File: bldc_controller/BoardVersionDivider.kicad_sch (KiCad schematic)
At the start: 2 parts

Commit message: might have fixed net issue, added dxf and svgs
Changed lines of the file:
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@@
     (stroke (width 0) (type default))
   )
-  (polyline (pts (xy 183.515 132.08) (xy 119.38 132.08))
-    (stroke (width 0) (type default))
-  )
-  (polyline (pts (xy 152.4 113.03) (xy 152.4 120.65))
+  (polyline (pts (xy 149.86 111.76) (xy 149.86 119.38))
     (stroke (width 0) (type default))
   )
@@
     (stroke (width 0) (type default))
   )
-  (polyline (pts (xy 187.325 59.69) (xy 187.325 128.27))
-    (stroke (width 0) (type default))
-  )
   (wire (pts (xy 162.56 83.82) (xy 149.86 83.82))
-    (stroke (width 0) (type default))
-  )
-  (polyline (pts (xy 119.38 55.88) (xy 183.515 55.88))
     (stroke (width 0) (type default))
   )
@@
     (stroke (width 0) (type default))
   )
-  (polyline (pts (xy 142.24 116.84) (xy 162.56 116.84))
+  (polyline (pts (xy 139.7 115.57) (xy 160.02 115.57))
     (stroke (width 0) (type default))
   )
@@
     (stroke (width 0) (type default))
   )
-  (polyline (pts (xy 115.57 59.69) (xy 115.57 128.27))
-    (stroke (width 0) (type default))
+  (rectangle (start 104.14 49.53) (end 198.12 133.35)
+    (stroke (width 1) (type default) (color 200 200 200 1))
+    (fill (type none))
   )
-  (arc (start 187.325 128.27) (mid 186.2108 130.9673) (end 183.515 132.08)
+  (rectangle (start 139.7 111.76) (end 160.02 119.38)
     (stroke (width 0) (type default))
     (fill (type none))
   )
-  (arc (start 183.515 55.88) (mid 186.2073 56.9962) (end 187.325 59.69)
-    (stroke (width 0) (type default))
-    (fill (type none))
-  )
-  (rectangle (start 142.24 113.03) (end 162.56 120.65)
-    (stroke (width 0) (type default))
-    (fill (type none))
-  )
-  (arc (start 115.57 59.69) (mid 116.6859 56.9959) (end 119.38 55.88)
-    (stroke (width 0) (type default))
-    (fill (type none))
-  )
-  (arc (start 119.38 132.08) (mid 116.6845 130.9655) (end 115.57 128.27)
-    (stroke (width 0) (type default))
-    (fill (type none))
-  )
-  (text_box "Necessary to be compatible with moteus FW."
-    (at 115.57 133.35 0) (size 71.12 11.43)
+  (text_box "100k"
+    (at 149.86 111.76 0) (size 10.16 3.81)
     (stroke (width -0.0001) (type default))
     (fill (type none))
-    (effects (font (size 2.54 2.54) (color 0 0 0 1)) (justify bottom))
+    (effects (font (face "Arial") (size 1.27 1.27) (color 0 0 0 1)))
   )
-  (text_box "			TOP		BOT\n\nr1.1 r1.2	  x		100k\n\n     r1.3	100k	  x"
-    (at 128.905 109.22 0) (size 33.02 8.89)
+  (text_box "DESIGN NOTE:\nNecessary to be compatible with moteus FW."
+    (at 119.38 71.12 0) (size 26.67 8.89)
+    (stroke (width 0.8) (type solid) (color 255 165 0 1))
+    (fill (type none))
+    (effects (font (face "Arial") (size 1.27 1.27) (color 0 0 0 1)) (justify left top))
+  )
+  (text_box "BOTTOM"
+    (at 149.86 107.95 0) (size 10.16 3.81)
     (stroke (width -0.0001) (type default))
     (fill (type none))
-    (effects (font (size 1.27 1.27)) (justify left top))
+    (effects (font (face "Arial") (size 1.27 1.27) (color 0 0 0 1)))
   )
-  (text_box "Back to Top Level"
-    (at 265.43 166.37 0) (size 19.05 14.605)
-    (stroke (width 0) (type default) (color 0 0 0 1))
-    (fill (type color) (color 0 0 0 0.1))
-    (effects (font (size 2.54 2.54) (thickness 0.508) bold (color 0 0 0 1)) (href "#1"))
+  (text_box "x"
+    (at 139.7 111.76 0) (size 10.16 3.81)
+    (stroke (width -0.0001) (type default))
+    (fill (type none))
+    (effects (font (face "Arial") (size 1.27 1.27) (color 0 0 0 1)))
+  )
+  (text_box "[10] Misc - Board Version Divider"
+    (at 78.74 16.51 0) (size 137.16 12.7)
+    (stroke (width -0.0001) (type default))
+    (fill (type none))
+    (effects (font (face "Times New Roman") (size 6 6) (thickness 1.2) bold (color 162 22 34 1)))
+  )
+  (text_box "r1.3"
+    (at 129.54 115.57 0) (size 10.16 3.81)
+    (stroke (width -0.0001) (type default))
+    (fill (type none))
+    (effects (font (face "Arial") (size 1.27 1.27) (color 0 0 0 1)) (justify right))
+  )
+  (text_box "100k"
+    (at 139.7 115.57 0) (size 10.16 3.81)
+    (stroke (width -0.0001) (type default))
+    (fill (type none))
+    (effects (font (face "Arial") (size 1.27 1.27) (color 0 0 0 1)))
+  )
+  (text_box "TOP"
+    (at 139.7 107.95 0) (size 10.16 3.81)
+    (stroke (width -0.0001) (type default))
+    (fill (type none))
+    (effects (font (face "Arial") (size 1.27 1.27) (color 0 0 0 1)))
+  )
+  (text_box "x"
+    (at 149.86 115.57 0) (size 10.16 3.81)
+    (stroke (width -0.0001) (type default))
+    (fill (type none))
+    (effects (font (face "Arial") (size 1.27 1.27) (color 0 0 0 1)))
   )
   (text_box "Board Version Resistor Divider"
-    (at 118.11 120.65 0) (size 66.675 9.525)
+    (at 105.41 121.92 0) (size 91.44 9.525)
     (stroke (width -0.0001) (type default))
     (fill (type none))
-    (effects (font (size 2.54 2.54) (thickness 0.508) bold (color 0 0 0 1)) (justify bottom))
+    (effects (font (face "Times New Roman") (size 2.54 2.54) (thickness 0.508) bold (color 162 22 34 1)) (justify bottom))
+  )
+  (text_box "r1.1, r1.2"
+    (at 129.54 111.76 0) (size 10.16 3.81)
+    (stroke (width -0.0001) (type default))
+    (fill (type none))
+    (effects (font (face "Arial") (size 1.27 1.27) (color 0 0 0 1)) (justify right))
   )
   (hierarchical_label "BOARD_VERSION" (shape output) (at 162.56 83.82 0) (fields_autoplaced)
@@
     (instances
       (project "bldc_controller"
-        (path "/0650c7a8-acba-429c-9f8e-eec0baf0bc1c/6ac64cfc-cd02-4504-88c7-a17dadca0833"
+        (path "/0650c7a8-acba-429c-9f8e-eec0baf0bc1c/fede4c36-00cc-4d3d-b71c-5243ba232202/07dcaf51-abc9-470d-8bd8-30b1c54b6fbd"
           (reference "R44") (unit 1)
         )
@@
   (symbol (lib_id "power:+3V3") (at 149.86 64.77 0) (unit 1)
     (in_bom yes) (on_board yes) (dnp no) (fields_autoplaced)
-    (property "Reference" "#PWR070" (at 149.86 68.58 0)
+    (property "Reference" "#PWR059" (at 149.86 68.58 0)
       (effects (font (size 1.27 1.27)) hide)
     )
@@
     (instances
       (project "bldc_controller"
-        (path "/0650c7a8-acba-429c-9f8e-eec0baf0bc1c/6ac64cfc-cd02-4504-88c7-a17dadca0833"
-          (reference "#PWR070") (unit 1)
+        (path "/0650c7a8-acba-429c-9f8e-eec0baf0bc1c/fede4c36-00cc-4d3d-b71c-5243ba232202/07dcaf51-abc9-470d-8bd8-30b1c54b6fbd"
+          (reference "#PWR059") (unit 1)
         )
       )
@@
   (symbol (lib_id "power:GND") (at 149.86 100.33 0) (unit 1)
     (in_bom yes) (on_board yes) (dnp no) (fields_autoplaced)
-    (property "Reference" "#PWR071" (at 149.86 106.68 0)
+    (property "Reference" "#PWR060" (at 149.86 106.68 0)
       (effects (font (size 1.27 1.27)) hide)
     )
@@
     (instances
       (project "bldc_controller"
-        (path "/0650c7a8-acba-429c-9f8e-eec0baf0bc1c/6ac64cfc-cd02-4504-88c7-a17dadca0833"
-          (reference "#PWR071") (unit 1)
+        (path "/0650c7a8-acba-429c-9f8e-eec0baf0bc1c/fede4c36-00cc-4d3d-b71c-5243ba232202/07dcaf51-abc9-470d-8bd8-30b1c54b6fbd"
+          (reference "#PWR060") (unit 1)
         )
       )
@@
     (instances
       (project "bldc_controller"
-        (path "/0650c7a8-acba-429c-9f8e-eec0baf0bc1c/6ac64cfc-cd02-4504-88c7-a17dadca0833"
+        (path "/0650c7a8-acba-429c-9f8e-eec0baf0bc1c/fede4c36-00cc-4d3d-b71c-5243ba232202/07dcaf51-abc9-470d-8bd8-30b1c54b6fbd"
           (reference "R43") (unit 1)
         )

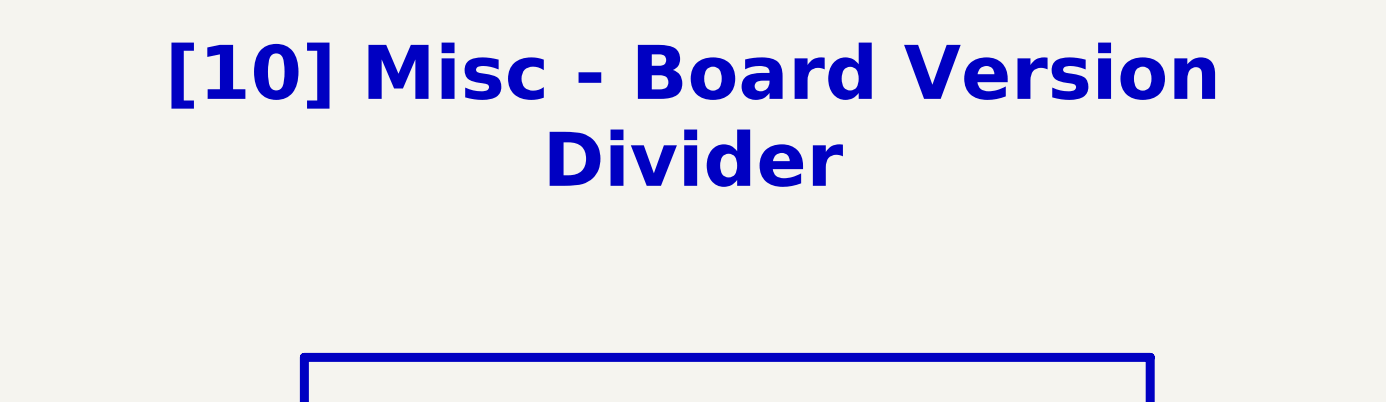
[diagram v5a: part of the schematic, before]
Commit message: Replaced 3v3 buck with WSON package alternative. Will back-annotate components
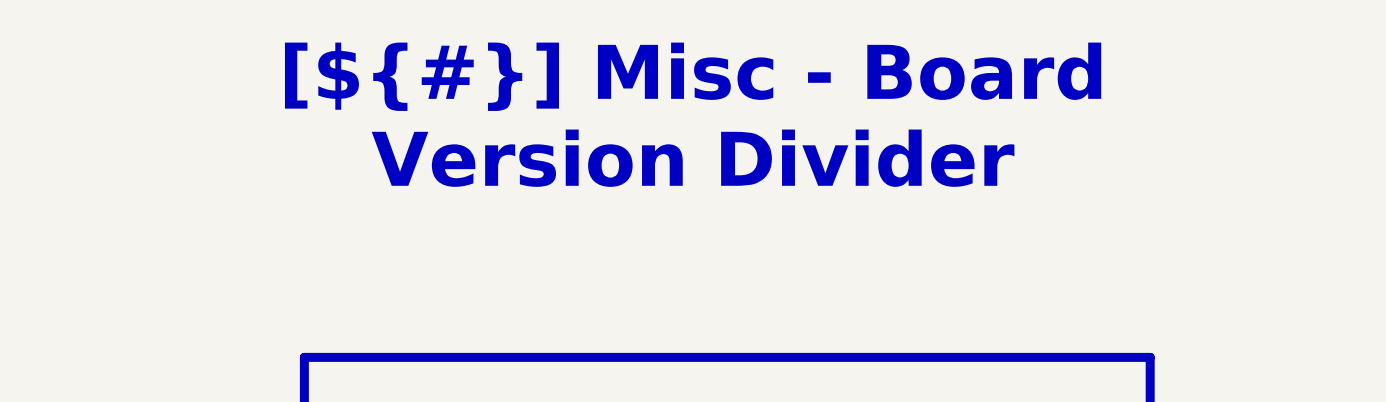
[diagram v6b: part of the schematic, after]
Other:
- company: EPFL Xplore -> ${COMPANY}
- title: Board Version Resistor Divider -> Misc - Board Version Divider
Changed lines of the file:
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@@
   (paper "A4")
   (title_block
-    (title "Board Version Resistor Divider")
+    (title "Misc - Board Version Divider")
     (date "2023-10-14")
-    (rev "1.0")
-    (company "EPFL Xplore")
-    (comment 3 "Author: Vincent Nguyen")
+    (rev "${REVISION}")
+    (company "${COMPANY}")
+    (comment 3 "Author: ${AUTHOR}")
   )
   (junction (at 149.86 83.82) (diameter 0) (color 0 0 0 0)
@@
   )
   (wire (pts (xy 149.86 100.33) (xy 149.86 96.52))
-    (stroke (width 0.381) (type default) (color 0 0 0 1))
+    (stroke (width 0) (type default))
   )
   (rectangle (start 104.14 49.53) (end 198.12 133.35)
@@
     (effects (font (face "Arial") (size 1.27 1.27) (color 0 0 0 1)))
   )
-  (text_box "[10] Misc - Board Version Divider"
+  (text_box "[${#}] ${TITLE}"
     (at 78.74 16.51 0) (size 137.16 12.7)
     (stroke (width -0.0001) (type default))

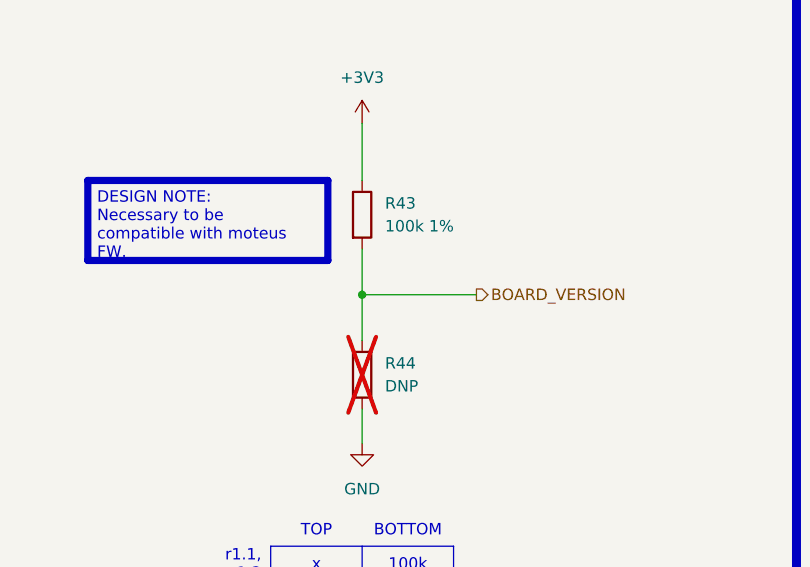
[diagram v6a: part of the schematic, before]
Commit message: routed all signals. TODO: redo all power polygons and ensure good return paths/reference. Added 3d models
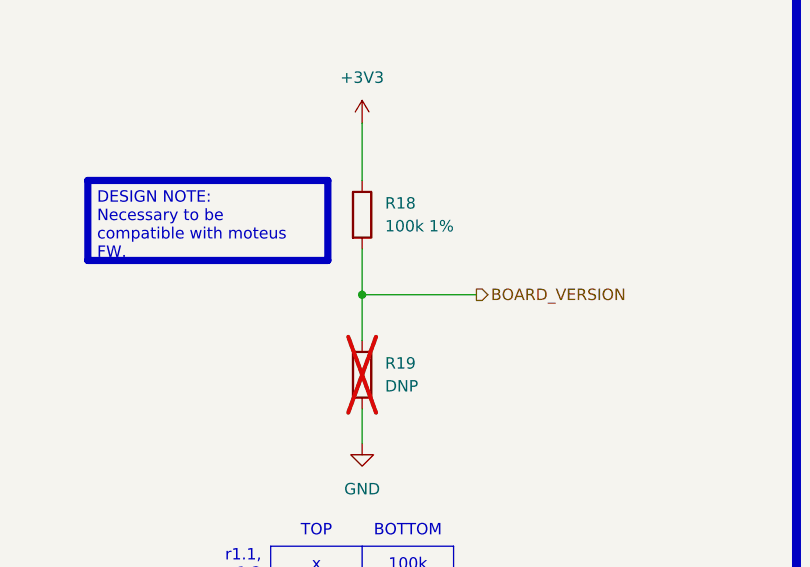
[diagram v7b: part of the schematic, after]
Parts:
- renumbered R43 to R18, R44 to R19
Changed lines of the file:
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@@
   (symbol (lib_id "Device:R") (at 149.86 92.71 0) (unit 1)
     (in_bom no) (on_board yes) (dnp yes) (fields_autoplaced)
-    (property "Reference" "R44" (at 152.4 91.44 0)
+    (property "Reference" "R19" (at 152.4 91.44 0)
       (effects (font (size 1.27 1.27)) (justify left))
     )
@@
       (project "bldc_controller"
         (path "/0650c7a8-acba-429c-9f8e-eec0baf0bc1c/fede4c36-00cc-4d3d-b71c-5243ba232202/07dcaf51-abc9-470d-8bd8-30b1c54b6fbd"
-          (reference "R44") (unit 1)
+          (reference "R19") (unit 1)
         )
       )
@@
   (symbol (lib_id "power:+3V3") (at 149.86 64.77 0) (unit 1)
     (in_bom yes) (on_board yes) (dnp no) (fields_autoplaced)
-    (property "Reference" "#PWR059" (at 149.86 68.58 0)
+    (property "Reference" "#PWR037" (at 149.86 68.58 0)
       (effects (font (size 1.27 1.27)) hide)
     )
@@
       (project "bldc_controller"
         (path "/0650c7a8-acba-429c-9f8e-eec0baf0bc1c/fede4c36-00cc-4d3d-b71c-5243ba232202/07dcaf51-abc9-470d-8bd8-30b1c54b6fbd"
-          (reference "#PWR059") (unit 1)
+          (reference "#PWR037") (unit 1)
         )
       )
@@
   (symbol (lib_id "power:GND") (at 149.86 100.33 0) (unit 1)
     (in_bom yes) (on_board yes) (dnp no) (fields_autoplaced)
-    (property "Reference" "#PWR060" (at 149.86 106.68 0)
+    (property "Reference" "#PWR038" (at 149.86 106.68 0)
       (effects (font (size 1.27 1.27)) hide)
     )
@@
       (project "bldc_controller"
         (path "/0650c7a8-acba-429c-9f8e-eec0baf0bc1c/fede4c36-00cc-4d3d-b71c-5243ba232202/07dcaf51-abc9-470d-8bd8-30b1c54b6fbd"
-          (reference "#PWR060") (unit 1)
+          (reference "#PWR038") (unit 1)
         )
       )
@@
   (symbol (lib_id "Device:R") (at 149.86 74.93 0) (unit 1)
     (in_bom yes) (on_board yes) (dnp no) (fields_autoplaced)
-    (property "Reference" "R43" (at 152.4 73.66 0)
+    (property "Reference" "R18" (at 152.4 73.66 0)
       (effects (font (size 1.27 1.27)) (justify left))
     )
@@
       (project "bldc_controller"
         (path "/0650c7a8-acba-429c-9f8e-eec0baf0bc1c/fede4c36-00cc-4d3d-b71c-5243ba232202/07dcaf51-abc9-470d-8bd8-30b1c54b6fbd"
-          (reference "R43") (unit 1)
+          (reference "R18") (unit 1)
         )
       )
